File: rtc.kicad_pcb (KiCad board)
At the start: 2 copper layers, 50 x 30 mm, 13 parts, among them J1 Conn_01x05, U1 DS1302N+, Y1 32.768kHz

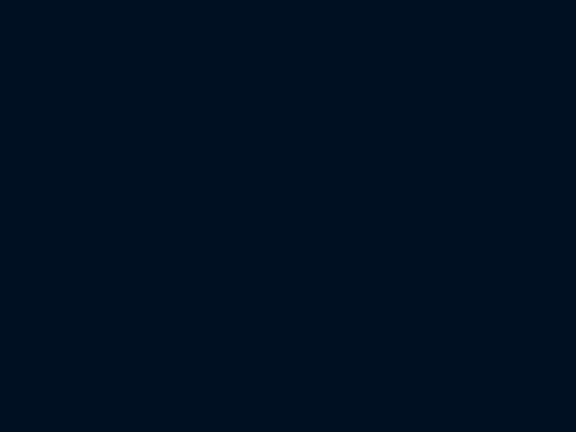
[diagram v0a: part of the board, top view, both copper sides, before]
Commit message: Remove redundant pull-ups per datasheet
- Capacitors accross crystal removed per datasheet info on oscillator circuit
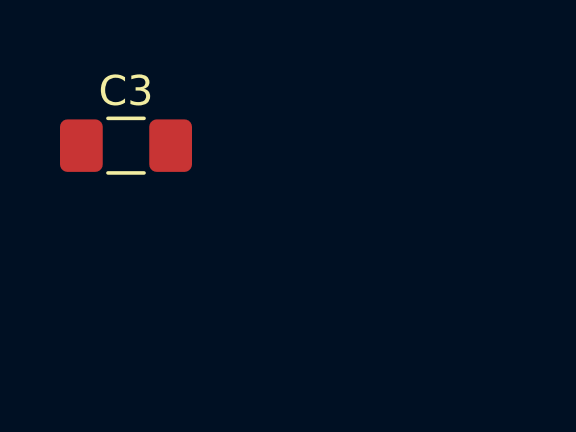
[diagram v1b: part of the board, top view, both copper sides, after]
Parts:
- added C3: 1uF, Capacitor_SMD:C_1206_3216Metric_Pad1.42x1.75mm_HandSolder, F.Cu at (18.3, 18.3)
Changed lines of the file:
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@@
     (tracks 40)
     (zones 0)
-    (modules 13)
+    (modules 14)
     (nets 9)
   )
@@
     (add_net "Net-(C2-Pad1)")
   )
-  (module MountingHole:MountingHole_3.2mm_M3_ISO7380 (layer F.Cu)
+  (module Capacitor_SMD:C_1206_3216Metric_Pad1.42x1.75mm_HandSolder (layer F.Cu)
+    (at 18.275001 18.345001)
+    (descr "Capacitor SMD 1206 (3216 Metric), square (rectangular) end terminal, IPC_7351 nominal with elongated pad for handsoldering. (Body size source: http://www.tortai-tech.com/upload/download/2011102023233369053.pdf), generated with kicad-footprint-generator")
+    (tags "capacitor handsolder")
+    (attr smd)
+    (fp_text reference C3 (at 0 -1.82) (layer F.SilkS)
+      (effects (font (size 1 1) (thickness 0.15)))
+    )
+    (fp_text value 1uF (at 0 1.82) (layer F.Fab)
+      (effects (font (size 1 1) (thickness 0.15)))
+    )
+    (fp_text user %R (at 0 0) (layer F.Fab)
+      (effects (font (size 0.8 0.8) (thickness 0.12)))
+    )
+    (fp_line (start 2.45 1.12) (end -2.45 1.12) (layer F.CrtYd) (width 0.05))
+    (fp_line (start 2.45 -1.12) (end 2.45 1.12) (layer F.CrtYd) (width 0.05))
+    (fp_line (start -2.45 -1.12) (end 2.45 -1.12) (layer F.CrtYd) (width 0.05))
+    (fp_line (start -2.45 1.12) (end -2.45 -1.12) (layer F.CrtYd) (width 0.05))
+    (fp_line (start -0.602064 0.91) (end 0.602064 0.91) (layer F.SilkS) (width 0.12))
+    (fp_line (start -0.602064 -0.91) (end 0.602064 -0.91) (layer F.SilkS) (width 0.12))
+    (fp_line (start 1.6 0.8) (end -1.6 0.8) (layer F.Fab) (width 0.1))
+    (fp_line (start 1.6 -0.8) (end 1.6 0.8) (layer F.Fab) (width 0.1))
+    (fp_line (start -1.6 -0.8) (end 1.6 -0.8) (layer F.Fab) (width 0.1))
+    (fp_line (start -1.6 0.8) (end -1.6 -0.8) (layer F.Fab) (width 0.1))
+    (pad 2 smd roundrect (at 1.4875 0) (size 1.425 1.75) (layers F.Cu F.Paste F.Mask) (roundrect_rratio 0.175439)
+      (net 1 GND))
+    (pad 1 smd roundrect (at -1.4875 0) (size 1.425 1.75) (layers F.Cu F.Paste F.Mask) (roundrect_rratio 0.175439)
+      (net 8 +5V))
+    (model ${KISYS3DMOD}/Capacitor_SMD.3dshapes/C_1206_3216Metric.wrl
+      (at (xyz 0 0 0))
+      (scale (xyz 1 1 1))
+      (rotate (xyz 0 0 0))
+    )
+  )
+  (module MountingHole:MountingHole_3.2mm_M3_ISO7380 locked (layer F.Cu)
     (at 29.4 34.4)
     (descr "Mounting Hole 3.2mm, no annular, M3, ISO7380")
@@
     (pad 1 np_thru_hole circle (at 0 0) (size 3.2 3.2) (drill 3.2) (layers *.Cu *.Mask))
   )
-  (module MountingHole:MountingHole_3.2mm_M3_ISO7380 (layer F.Cu)
+  (module MountingHole:MountingHole_3.2mm_M3_ISO7380 locked (layer F.Cu)
     (at 29.4 57.6)
     (descr "Mounting Hole 3.2mm, no annular, M3, ISO7380")
@@
     (pad 1 np_thru_hole circle (at 0 0) (size 3.2 3.2) (drill 3.2) (layers *.Cu *.Mask))
   )
-  (module MountingHole:MountingHole_3.2mm_M3_ISO7380 (layer F.Cu)
+  (module MountingHole:MountingHole_3.2mm_M3_ISO7380 locked (layer F.Cu)
     (at 72.6 57.6)
     (descr "Mounting Hole 3.2mm, no annular, M3, ISO7380")
@@
     (pad 1 np_thru_hole circle (at 0 0) (size 3.2 3.2) (drill 3.2) (layers *.Cu *.Mask))
   )
-  (module MountingHole:MountingHole_3.2mm_M3_ISO7380 (layer F.Cu)
+  (module MountingHole:MountingHole_3.2mm_M3_ISO7380 locked (layer F.Cu)
     (at 72.6 34.4)
     (descr "Mounting Hole 3.2mm, no annular, M3, ISO7380")

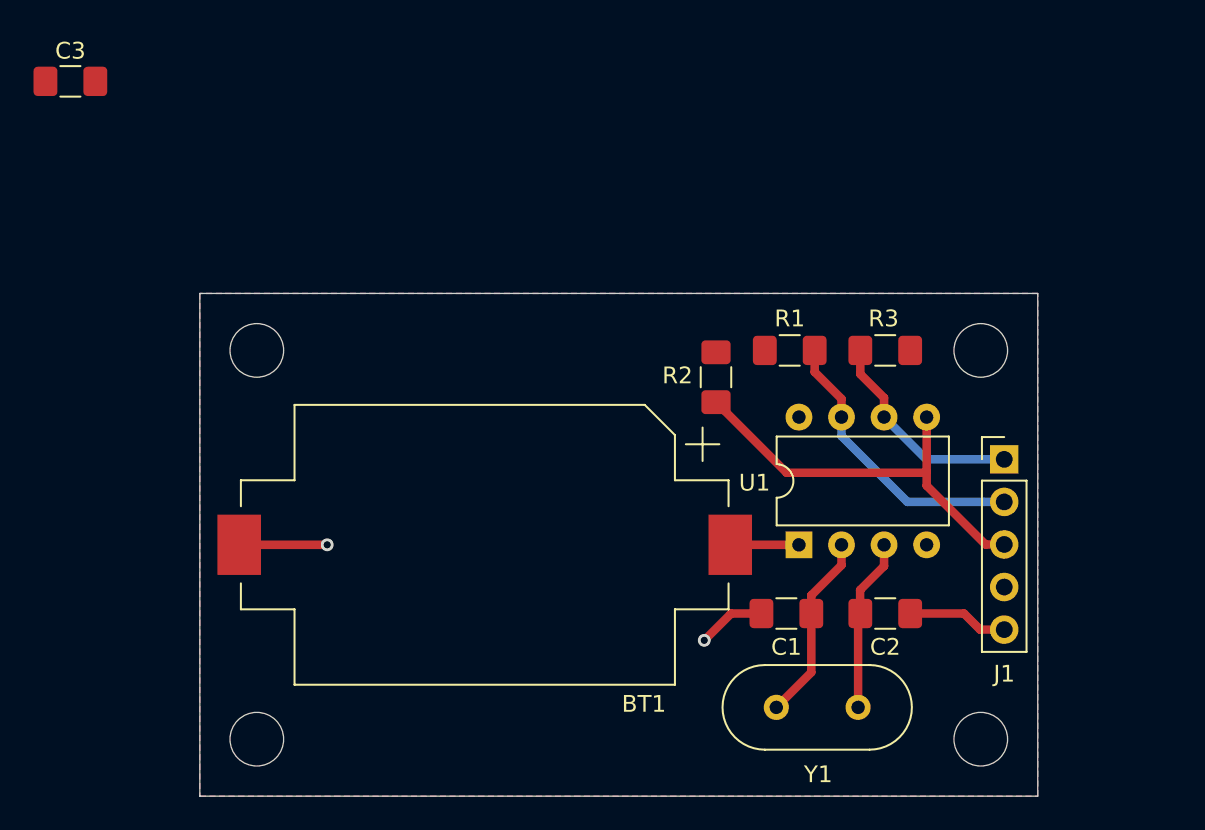
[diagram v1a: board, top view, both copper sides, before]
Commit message: Simplify by removing pull-ups and bypass cap per datasheet
- Re-run traces
- Update img/readme
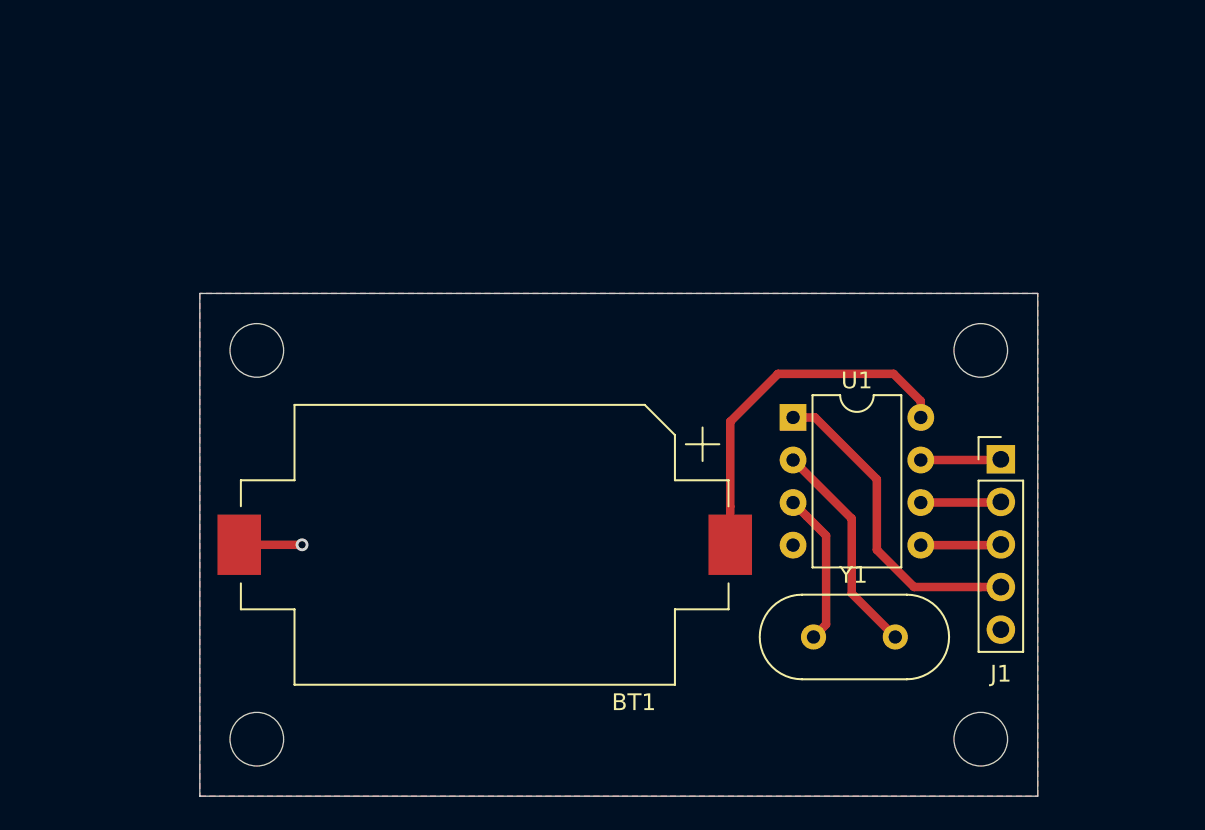
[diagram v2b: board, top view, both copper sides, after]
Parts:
- removed C1, C2: 22pF, Capacitor_SMD:C_1206_3216Metric_Pad1.42x1.75mm_HandSolder
- removed C3: 1uF, Capacitor_SMD:C_1206_3216Metric_Pad1.42x1.75mm_HandSolder
- removed R1, R2, R3: 10k, Resistor_SMD:R_1206_3216Metric_Pad1.42x1.75mm_HandSolder
- moved Y1 8.25 mm to (67.5, 51.5), turned to 180 degrees
- moved U1 7.61 mm to (61.4, 38.4), turned to 0 degrees
- moved J1 0.20 mm to (73.8, 40.9)
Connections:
- net /RST renamed /CE
- J1 pad 1: /SCL -> /SCLK
- J1 pad 2: /SDA -> /IO
- U1 pad 1: Net-(BT1-Pad1) -> +5V
- U1 pad 6: /SCL -> /IO
- U1 pad 7: /SDA -> /SCLK
- U1 pad 8: +5V -> Net-(BT1-Pad1)
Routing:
- net /CE: track 24.8 -> 4.80 mm
- net +5V: track 0.00 -> 19.1 mm
- net Net-(BT1-Pad1): track 4.10 -> 21.6 mm
- net /SDA: track 17.1 -> 0.00 mm
- net /SCL: track 12.8 -> 0.00 mm
- net GND: track 15.3 -> 3.75 mm, vias 2 -> 1
- net /SCLK: track 0.00 -> 4.80 mm
- net /IO: track 0.00 -> 4.80 mm
- net Net-(U1-Pad2): track 11.3 -> 13.1 mm
- net Net-(U1-Pad3): track 10.4 -> 9.15 mm
- added copper zone on F.Cu, net GND
- removed copper zone on F.Cu, net +5V

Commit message: Remove front copper polygon fill
- Clean up labels
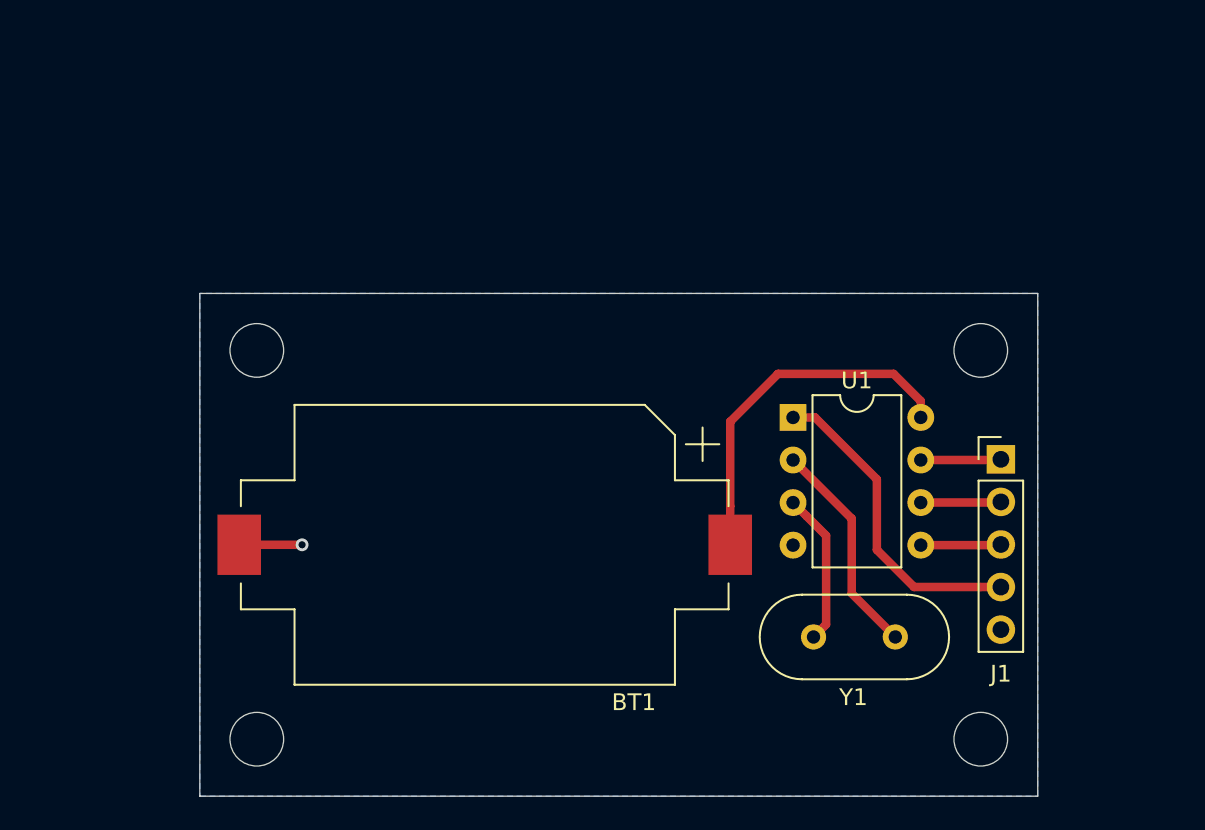
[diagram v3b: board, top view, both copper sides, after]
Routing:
- removed copper zone on F.Cu, net GND
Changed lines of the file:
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@@
     (descr "Crystal THT HC-49/U http://5hertz.com/pdfs/04404_D.pdf")
     (tags "THT crystalHC-49/U")
-    (fp_text reference Y1 (at 2.5 3.7) (layer F.SilkS)
+    (fp_text reference Y1 (at 2.5 -3.6) (layer F.SilkS)
       (effects (font (size 1 1) (thickness 0.15)))
     )
@@
     (connect_pads (clearance 0.508))
     (min_thickness 0.254)
-    (fill yes (arc_segments 32) (thermal_gap 0.508) (thermal_bridge_width 0.508))
-    (polygon
-      (pts
-        (xy 26 31) (xy 26 61) (xy 76 61) (xy 76 31)
-      )
-    )
-  )
-  (zone (net 1) (net_name GND) (layer F.Cu) (hatch edge 0.508)
-    (connect_pads (clearance 0.508))
-    (min_thickness 0.254)

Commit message: Redo pcb layout and traces
- Restored front copper polygon fill
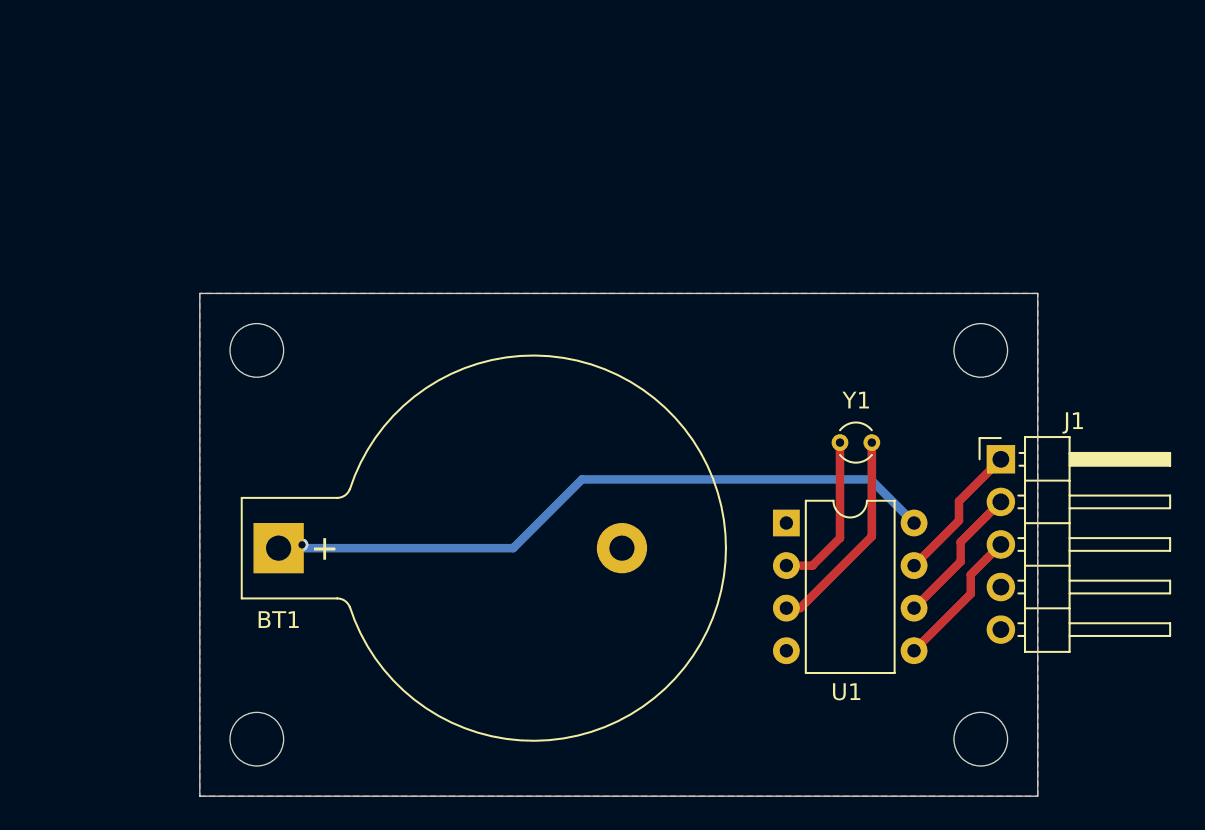
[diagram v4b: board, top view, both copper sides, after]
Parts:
- BT1: value Battery_Cell -> CR2032; footprint Battery:BatteryHolder_Keystone_1060_1x2032 -> Battery:BatteryHolder_Keystone_103_1x20mm
- J1: footprint Connector_PinHeader_2.54mm:PinHeader_1x05_P2.54mm_Vertical -> Connector_PinHeader_2.54mm:PinHeader_1x05_P2.54mm_Horizontal
- Y1: footprint Crystal:Crystal_HC49-U_Vertical -> Crystal:Crystal_Round_D2.0mm_Vertical
- moved BT1 12.3 mm to (30.7, 46.2), turned to 0 degrees
- moved Y1 12.1 mm to (64.2, 39.9), turned to 0 degrees
- moved U1 6.31 mm to (61.0, 44.7)
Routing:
- net Net-(BT1-Pad1): track 21.6 -> 40.7 mm, vias 0 -> 1
- net +5V: track 19.1 -> 0.00 mm
- net GND: track 3.75 -> 0.00 mm, vias 1 -> 0
- net /SCLK: track 4.80 -> 8.49 mm
- net /IO: track 4.80 -> 8.49 mm
- net /CE: track 4.80 -> 8.49 mm
- net Net-(U1-Pad2): track 13.1 -> 9.58 mm
- net Net-(U1-Pad3): track 9.15 -> 12.5 mm
- added copper zone on F.Cu, net +5V
